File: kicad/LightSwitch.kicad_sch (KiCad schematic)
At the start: 31 parts, among them J1 Screw_Terminal_01x02, J2 Conn_01x03_Male, Q1 MMBT2222A, SW1 SW_Push_LED, SW2 SW_Push_LED, SW3 SW_Push_LED, SW4 SW_Push_LED, SW5 SW_Push_LED, U1 LM2936-3.3, U2 SHT35-DIS, U3 ATtiny806-S

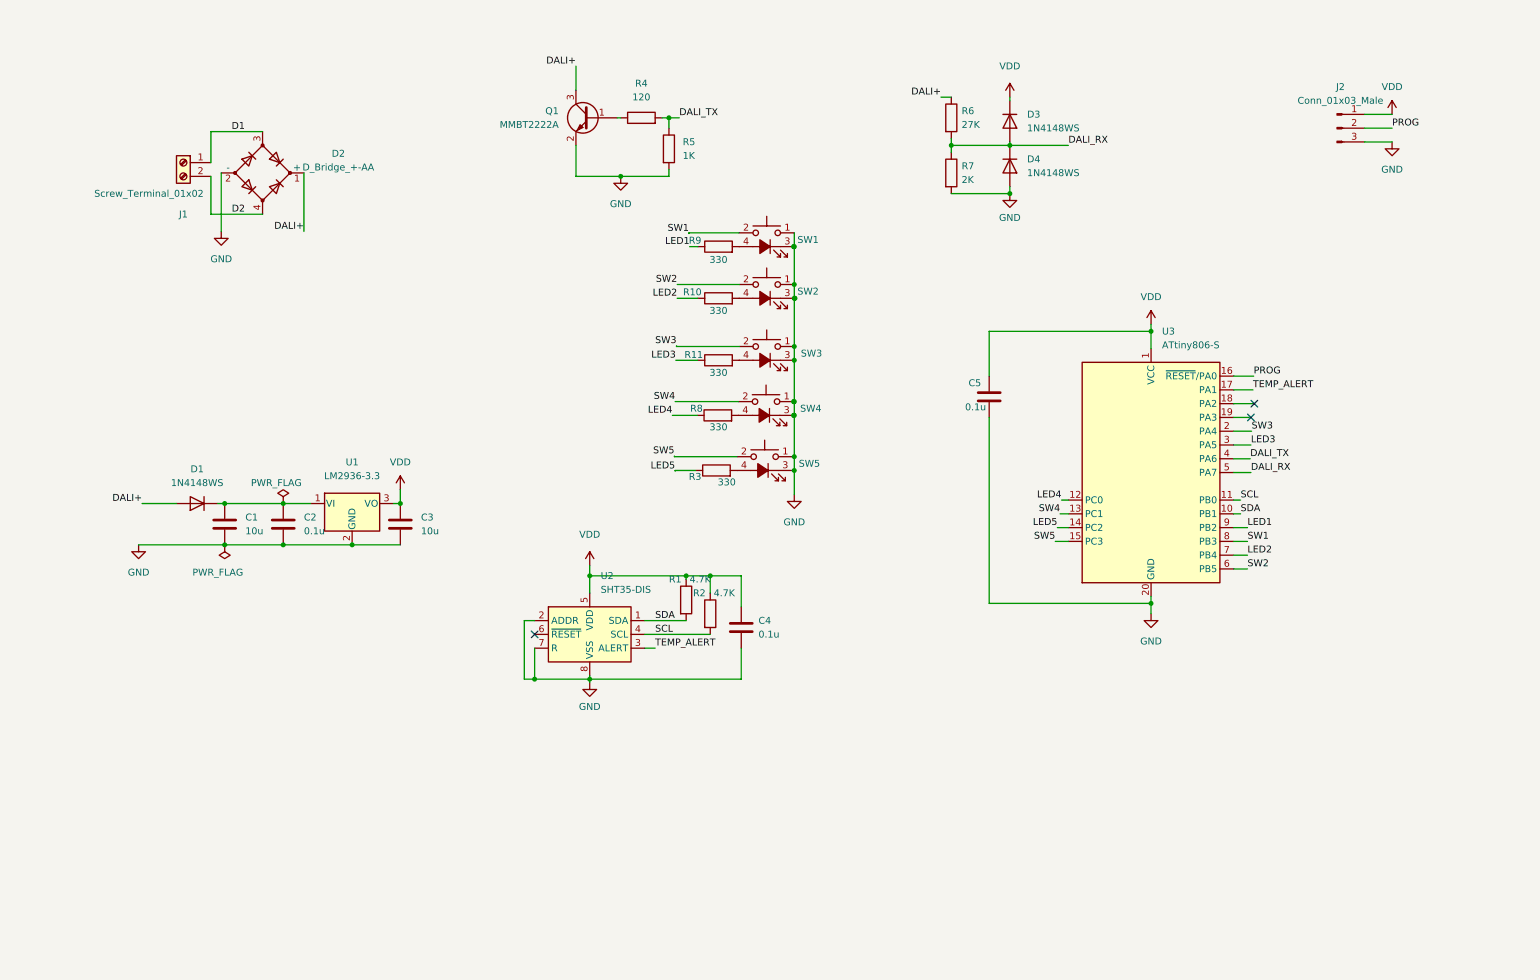
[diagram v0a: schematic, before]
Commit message: Updated with NRF52840 version. Modded since sending to OSHPark
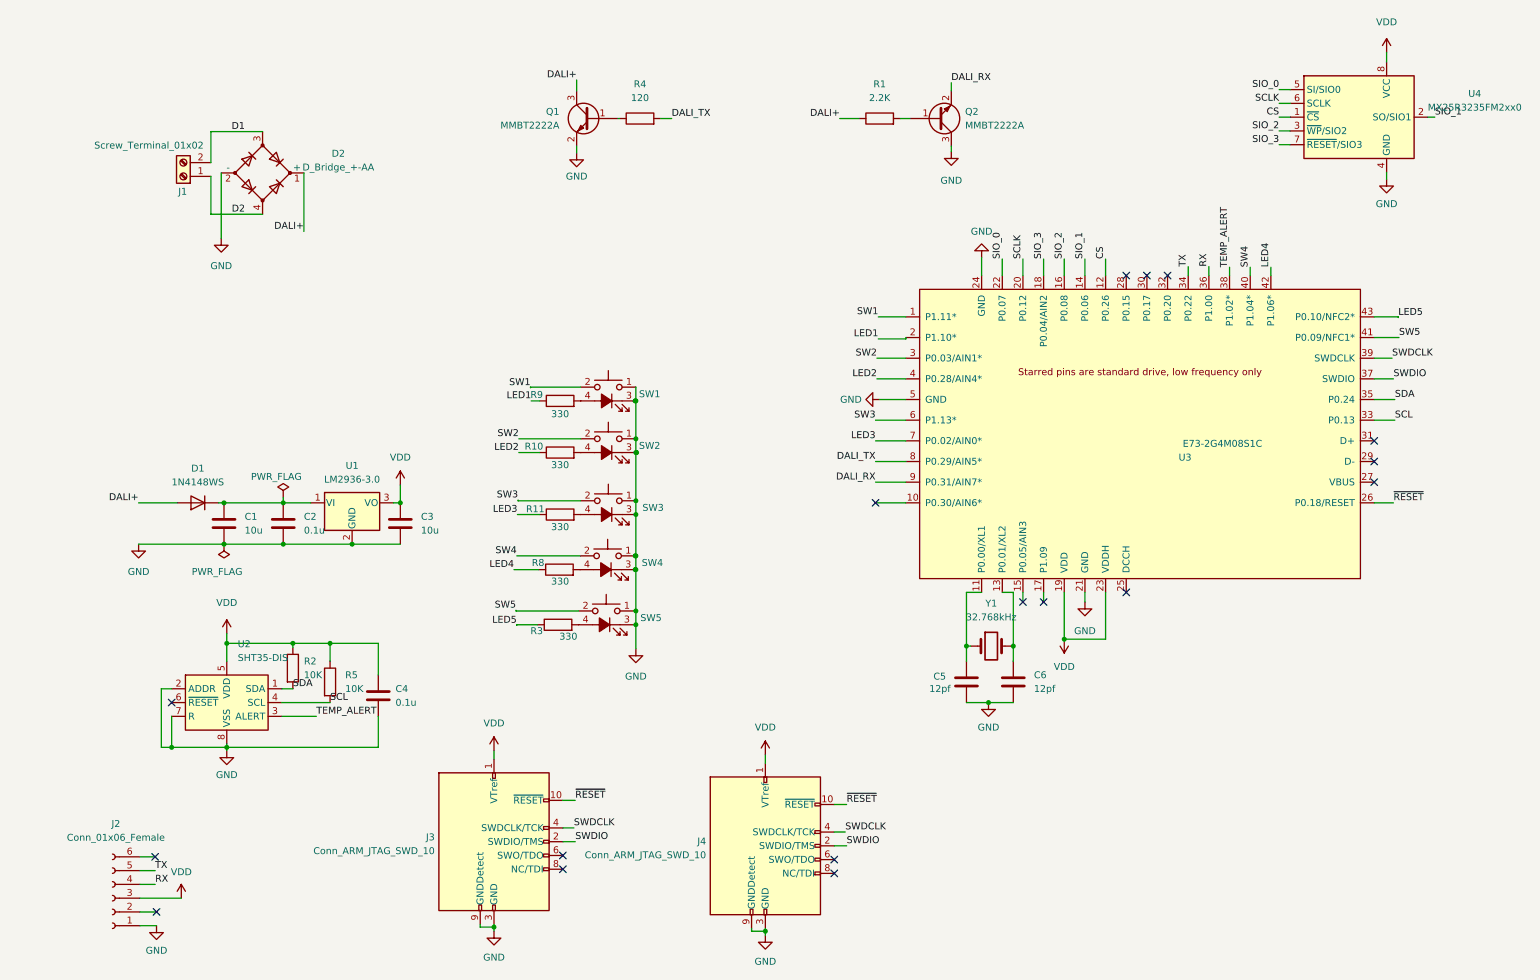
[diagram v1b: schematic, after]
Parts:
- removed D3, D4: 1N4148WS, Diode_SMD:D_SOD-323, symbol Diode:1N4148WS
- removed J2: Conn_01x03_Male, Connector_PinHeader_2.54mm:PinHeader_1x03_P2.54mm_Vertical, symbol Connector:Conn_01x03_Male
- removed R6: 27K, Resistor_SMD:R_0805_2012Metric, symbol Device:R
- removed R7: 2K, Resistor_SMD:R_0805_2012Metric, symbol Device:R
- removed U1: LM2936-3.3, Package_TO_SOT_SMD:SOT-223, symbol Regulator_Linear:LM2936-3.3
- removed U3: ATtiny806-S, Package_SO:SOIC-20W_7.5x12.8mm_P1.27mm, symbol MCU_Microchip_ATtiny:ATtiny806-S
- added C6: 12pf, Capacitor_SMD:C_0805_2012Metric, symbol Device:C
- added J2: Conn_01x06_Female, Connector_PinSocket_2.54mm:PinSocket_1x06_P2.54mm_Vertical, symbol Connector:Conn_01x06_Female
- added J3: Conn_ARM_JTAG_SWD_10, Connector_PinHeader_1.27mm:PinHeader_2x05_P1.27mm_Vertical_SMD, symbol Connector:Conn_ARM_JTAG_SWD_10
- added J4: Conn_ARM_JTAG_SWD_10, Connector:Tag-Connect_TC2050-IDC-NL_2x05_P1.27mm_Vertical, symbol Connector:Conn_ARM_JTAG_SWD_10
- added Q2: MMBT2222A, Package_TO_SOT_SMD:SOT-23, symbol Device:Q_NPN_BEC
- added U1: LM2936-3.0, Package_TO_SOT_THT:TO-92_Inline, symbol Regulator_Linear:LM2936-3.0
- added U3: E73-2G4M08S1C, E73-2G4M08S1C:E73-2G4M08S1C, symbol CDEbyte E73-2G4M08S1C:E73-2G4M08S1C
- added U4: MX25R3235FM2xx0, Package_SO:SOP-8_5.28x5.23mm_P1.27mm, symbol Memory_Flash:MX25R3235FM2xx0
- added Y1: 32.768kHz, Crystal:Crystal_SMD_3215-2Pin_3.2x1.5mm, symbol Device:Crystal
- C5: value 0.1u -> 12pf
- R1: value 4.7K -> 2.2K
- R2: value 4.7K -> 10K
- R5: value 1K -> 10K
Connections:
- net D1: now also J1.2 (Pin_2); no longer J1.1 (Pin_1)
- net D2: now also J1.1 (Pin_1); no longer J1.2 (Pin_2)
- net DALI+: now also R1.1
- net DALI_RX: now also Q2.2 (E), U3.9 (P0.31/AIN7*)
- net DALI_TX: now also U3.8 (P0.29/AIN5*); no longer R5.1
- net GND: now also C5.2, C6.2, J2.1 (Pin_1), J3.3 (GND), J3.5 (GND), J3.9 (GNDDetect), J4.3 (GND), J4.5 (GND), J4.9 (GNDDetect), Q2.3 (C), U1.2 (GND), U3.21 (GND), U3.24 (GND), U3.5 (GND), U4.4 (GND); no longer C5.1, R5.2
- net LED1: now also U3.2 (P1.10*)
- net LED2: now also U3.4 (P0.28/AIN4*)
- net LED3: now also U3.7 (P0.02/AIN0*)
- net LED4: now also U3.42 (P1.06*)
- net LED5: now also U3.43 (P0.10/NFC2*)
- net SCL: now also R5.2, U3.33 (P0.13); no longer R2.2
- net SDA: now also R2.2, U3.35 (P0.24); no longer R1.2
- net SW1: now also U3.1 (P1.11*)
- net SW2: now also U3.3 (P0.03/AIN1*)
- net SW3: now also U3.6 (P1.13*)
- net SW4: now also U3.40 (P1.04*)
- net SW5: now also U3.41 (P0.09/NFC1*)
- net TEMP_ALERT: now also U3.38 (P1.02*)
- net VDD: now also R5.1, J2.3 (Pin_3), J3.1 (VTref), J4.1 (VTref), U1.3 (VO), U3.19 (VDD), U3.23 (VDDH), U4.8 (VCC); no longer C5.2, R1.1
- net at C1.1, C2.1, D1.1 (K): now also U1.1 (VI)
- new net: C5.1, U3.11 (P0.00/XL1), Y1.1
- new net: C6.1, U3.13 (P0.01/XL2), Y1.2
- new net: Q2.1 (B), R1.2
- new net CS: U3.12 (P0.26), U4.1 (~{CS})
- new net RX: J2.4 (Pin_4), U3.36 (P1.00)
- new net SCLK: U3.20 (P0.12), U4.6 (SCLK)
- new net SIO_0: U3.22 (P0.07), U4.5 (SI/SIO0)
- new net SIO_1: U3.14 (P0.06), U4.2 (SO/SIO1)
- new net SIO_2: U3.16 (P0.08), U4.3 (~{WP}/SIO2)
- new net SIO_3: U3.18 (P0.04/AIN2), U4.7 (~{RESET}/SIO3)
- new net SWDCLK: J3.4 (SWDCLK/TCK), J4.4 (SWDCLK/TCK), U3.39 (SWDCLK)
- new net SWDIO: J3.2 (SWDIO/TMS), J4.2 (SWDIO/TMS), U3.37 (SWDIO)
- new net TX: J2.5 (Pin_5), U3.34 (P0.22)
- new net ~{RESET}: J3.10 (~{RESET}), J4.10 (~{RESET}), U3.26 (P0.18/RESET)
- no-connect marks 3 -> 17
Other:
- moved on the sheet: C4, J1, R10, R11, R3, R8, R9, SW1, SW2, SW3, SW4, SW5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

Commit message: latect schematic
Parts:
- removed C6: 12pf, Capacitor_SMD:C_0805_2012Metric, symbol Device:C
- removed J2: Conn_01x06_Female, Connector_PinSocket_2.54mm:PinSocket_1x06_P2.54mm_Vertical, symbol Connector:Conn_01x06_Female
- removed J3: Conn_ARM_JTAG_SWD_10, Connector_PinHeader_1.27mm:PinHeader_2x05_P1.27mm_Vertical_SMD, symbol Connector:Conn_ARM_JTAG_SWD_10
- removed J4: Conn_ARM_JTAG_SWD_10, Connector:Tag-Connect_TC2050-IDC-NL_2x05_P1.27mm_Vertical, symbol Connector:Conn_ARM_JTAG_SWD_10
- removed Q2: MMBT2222A, Package_TO_SOT_SMD:SOT-23, symbol Device:Q_NPN_BEC
- removed R10, R11, R8, R9: 330, Resistor_SMD:R_0805_2012Metric, symbol Device:R
- removed SW1, SW2, SW3, SW4, SW5: SW_Push_LED, LocalProject:LED Pushbutton, symbol Switch:SW_Push_LED
- removed U2: SHT35-DIS, Sensor_Humidity:Sensirion_DFN-8-1EP_2.5x2.5mm_P0.5mm_EP1.1x1.7mm, symbol Sensor_Humidity:SHT35-DIS
- removed U3: E73-2G4M08S1C, E73-2G4M08S1C:E73-2G4M08S1C, symbol CDEbyte E73-2G4M08S1C:E73-2G4M08S1C
- removed U4: MX25R3235FM2xx0, Package_SO:SOP-8_5.28x5.23mm_P1.27mm, symbol Memory_Flash:MX25R3235FM2xx0
- removed Y1: 32.768kHz, Crystal:Crystal_SMD_3215-2Pin_3.2x1.5mm, symbol Device:Crystal
- added D3: 30V, symbol Device:D_Zener
- added D?: Q_SCR_GAK, symbol Device:Q_SCR_GAK
- added F1: Fuse, symbol Device:Fuse
- added J2: Programming Header, symbol Connector_Generic:Conn_02x03_Odd_Even
- added R6: 470, Connector:Tag-Connect_TC2030-IDC-NL_2x03_P1.27mm_Vertical, symbol Device:R
- added SW1, SW2, SW3, SW4, SW5: SW_MEC_5E, symbol Switch:SW_MEC_5E
- added TP1, TP2, TP3, TP4: TestPoint, symbol Connector:TestPoint
- added U2: ATtiny807-M, Package_DFN_QFN:QFN-24-1EP_4x4mm_P0.5mm_EP2.6x2.6mm, symbol MCU_Microchip_ATtiny:ATtiny807-M
- added U3: OPA376xxDBV, Package_TO_SOT_SMD:SOT-23-5, symbol Amplifier_Operational:OPA376xxDBV
- C3: value 10u -> 47u
- C4: value 0.1u -> C
- C5: value 12pf -> 0.1u; footprint Capacitor_SMD:C_0805_2012Metric -> (none)
- R1: value 2.2K -> 0; footprint Resistor_SMD:R_0805_2012Metric -> (none)
- R2: value 10K -> 1K; footprint Resistor_SMD:R_0805_2012Metric -> (none)
- R3: value 330 -> 200K; footprint Resistor_SMD:R_0805_2012Metric -> (none)
- R4: value 120 -> 330
- R5: value 10K -> 27K; footprint Resistor_SMD:R_0805_2012Metric -> (none)
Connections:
- net LED5 is gone; now on net DALI+: R3.1
- net SCL is gone; now on net GND: R5.2
- net SDA is gone; now on net GND: R2.2
- net DALI+: now also D3.1 (K), D?.2 (A); no longer R1.1
- net DALI_RX: now also TP4.1, U2.11 (PB5), U3.1, U3.4 (-)
- net DALI_TX: now also TP3.1, U2.16 (PB0)
- net GND: now also C4.2, D?.3 (K), J2.6 (Pin_6), SW1.4 (A), SW2.4 (A), SW3.4 (A), SW4.4 (A), SW5.4 (A), U2.25 (GND), U2.3 (GND), U3.2 (V-); no longer C4.1
- net SW1: now also SW1.1, U2.1 (PA2)
- net SW2: now also SW2.1, U2.7 (PA6)
- net SW3: now also SW3.1, U2.14 (PB2)
- net SW4: now also SW4.1, U2.10 (PB6)
- net SW5: now also SW5.1, U2.19 (PC2)
- net VDD: now also C4.1, J2.2 (Pin_2), U2.4 (VCC), U3.5 (V+); no longer C4.2, R2.1, R5.1
- net at R3.2: now also R5.1, U3.3 (+)
- net at C5.1: now also R2.1, D3.2 (A), D?.1 (G)
- net at R1.2: now also D2.3, TP2.1
- net D1: no longer names the net of J1.2 (Pin_2)
- net D1: now also F1.1; no longer D2.3
- net D2: no longer names the net of D2.4, J1.1 (Pin_1)
- new net: F1.2, R1.1, TP1.1
- new net: R6.1, U2.23 (~{RESET}/PA0)
- new net DEBUG_OUT: J2.3 (Pin_3), U2.24 (PA1)
- new net UPDI: J2.1 (Pin_1), R6.2
- no-connect marks 17 -> 25
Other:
- moved on the sheet: D2, J1, Q1, R4
